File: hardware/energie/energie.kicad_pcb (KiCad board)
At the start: 2 copper layers, 102 x 87 mm, 86 parts, among them J1 transfos, J2 Conn_01x05_Pin, J3 linky, J4 Serial, J5 pilotes, J6 gpio, J7 I2C, J8 power, Q1 BSS123, Q2 BSS123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

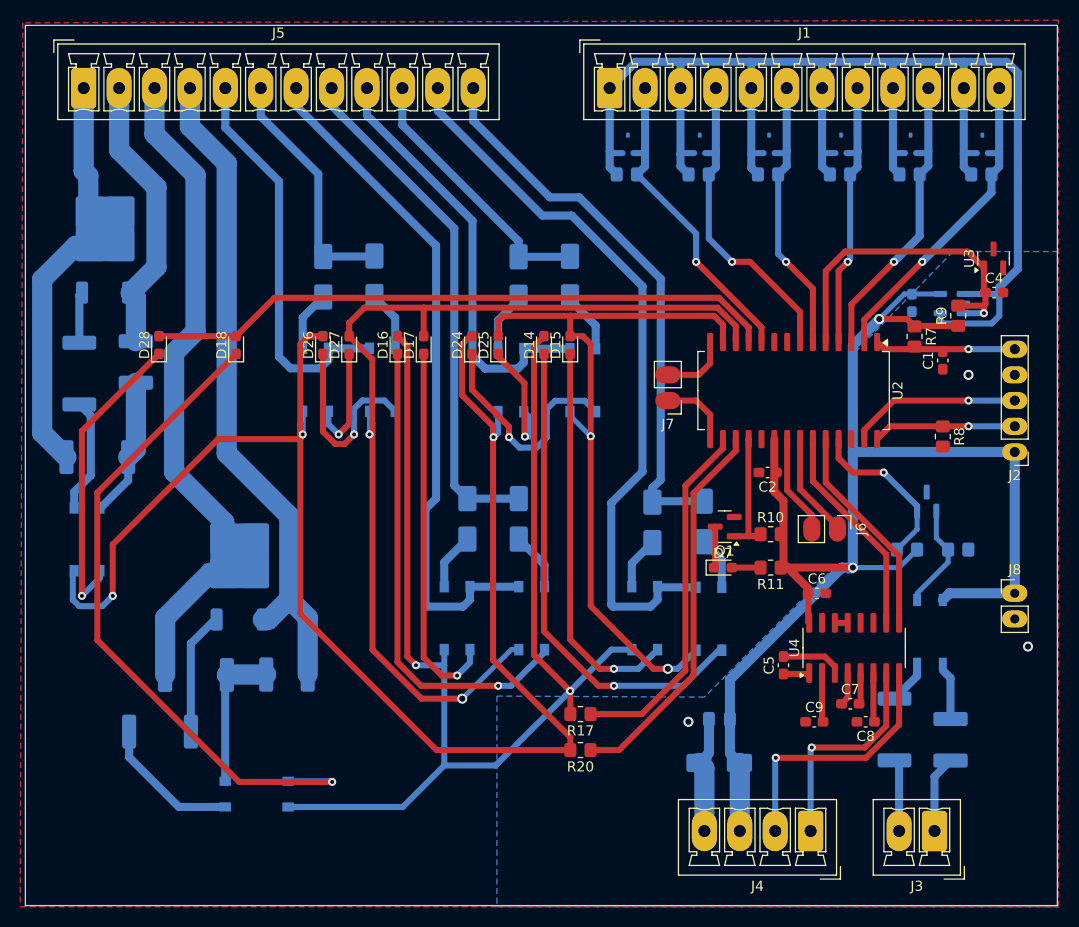
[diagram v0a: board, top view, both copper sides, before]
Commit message: energie: ajout d'une alimentation AC/DC pour que le module soit autonome (et que la connection à la centrale puisse être isolée)
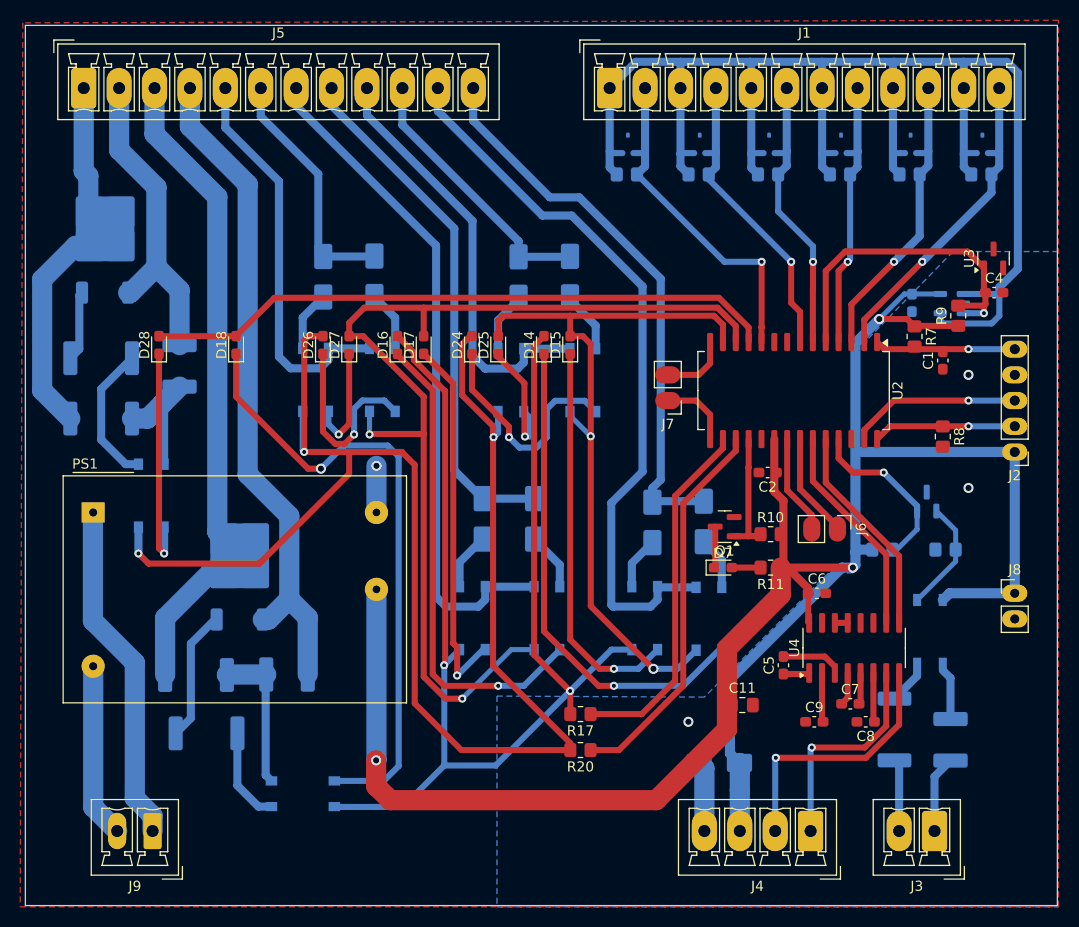
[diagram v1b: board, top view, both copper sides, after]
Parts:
- added J9: ACin, Connector_Phoenix_MC:PhoenixContact_MCV_1,5_2-G-3.5_1x02_P3.50mm_Vertical, F.Cu at (88.8, 130.4)
- added PS1: IRM-02-5, Converter_ACDC:Converter_ACDC_MeanWell_IRM-02-xx_THT, F.Cu at (82.9, 98.9)
- C11: moved to F.Cu
- moved U13 7.68 mm to (88.6, 97.3)
- moved R16 4.60 mm to (94.1, 120.8), turned to 0 degrees
- moved U8 4.57 mm to (103.6, 126.7)
- moved C13 4.33 mm to (91.4, 84.5)
- moved R18 3.83 mm to (83.7, 89.7)
- moved C11 2.66 mm to (147.1, 118.0), turned to 0 degrees
- moved R19 2.64 mm to (83.7, 83.7), turned to 0 degrees
- moved R12 2.43 mm to (160.9, 102.6), turned to 0 degrees
- moved U10 1.51 mm to (127.8, 109.4)
- moved U7 1.51 mm to (120.4, 109.4)
- moved D12 1.51 mm to (126.5, 99.6)
- moved D13 1.51 mm to (121.4, 99.6)
- moved R13 1.25 mm to (167.1, 102.6), turned to 180 degrees
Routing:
- net +5V: track 143.3 -> 213.3 mm, vias 2 -> 3
- net Net-(J9-Pin_1): track 0.00 -> 33.9 mm
- net Net-(J9-Pin_2): track 0.00 -> 17.3 mm
- net Net-(D28-K): track 30.3 -> 22.5 mm
- net /outputs/OB: track 98.0 -> 104.3 mm
- net Net-(D14-A): track 126.9 -> 121.4 mm
- net Net-(D18-K): track 67.4 -> 62.2 mm
- net Net-(R16-Pad2): track 14.1 -> 9.39 mm
- net Net-(D19-A1): track 27.8 -> 31.7 mm
- net Net-(D19-A2): track 36.9 -> 33.3 mm
- net Net-(R19-Pad2): track 11.4 -> 14.0 mm
- net Net-(J1-Pin_2): track 31.8 -> 33.9 mm
- net Net-(D19-G): track 5.06 -> 6.96 mm
- net Net-(C13-Pad2): track 13.9 -> 12.0 mm
- net Net-(D9-A2): track 62.5 -> 60.7 mm
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
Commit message: Utilise des emprumtes CMS pour deux connecteurs optionels.
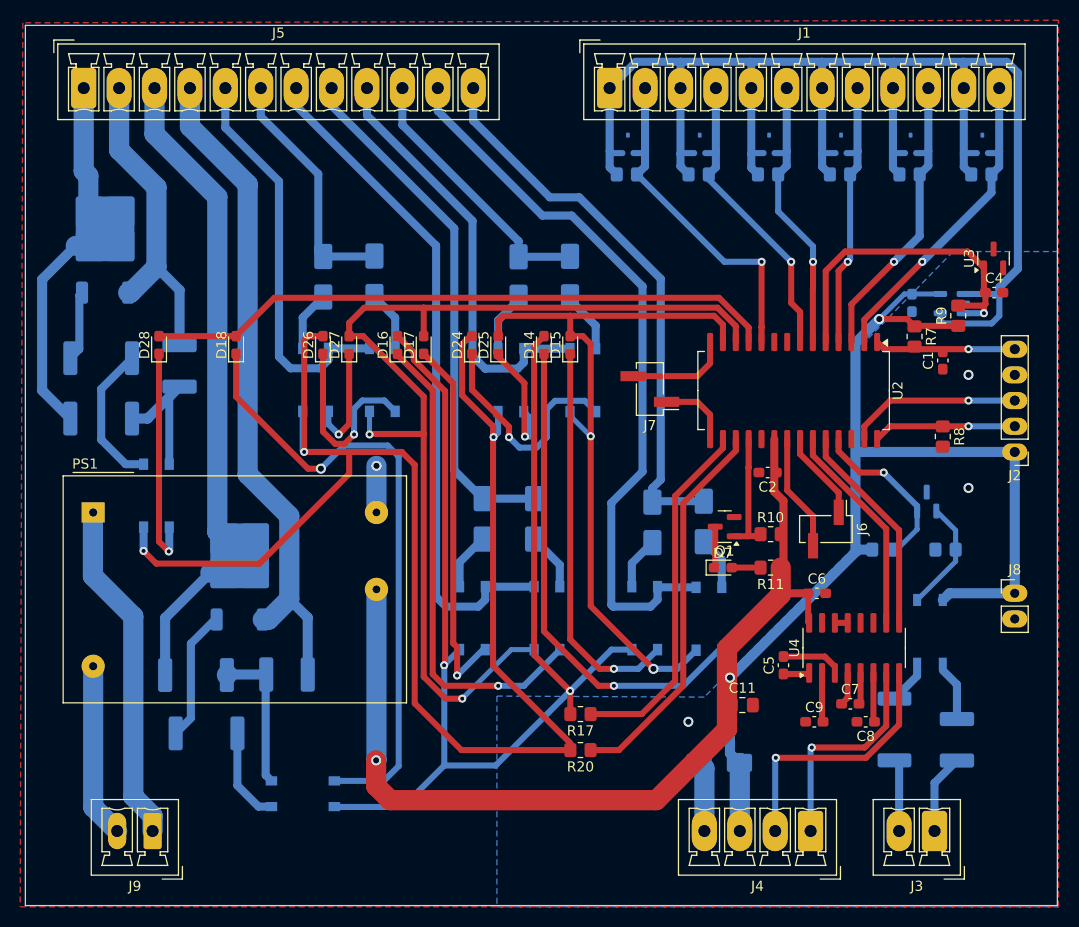
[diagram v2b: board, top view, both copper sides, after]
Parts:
- J6, J7: footprint Connector_PinHeader_2.54mm:PinHeader_1x02_P2.54mm_Vertical -> Connector_PinHeader_2.54mm:PinHeader_1x02_P2.54mm_Vertical_SMD_Pin1Left
- moved J7 2.11 mm to (137.9, 86.7)
- moved J6 1.14 mm to (155.3, 100.6)
- moved C10 0.64 mm to (168.3, 121.4)
- moved U13 0.51 mm to (89.2, 97.3)
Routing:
- net +5V: track 213.3 -> 208.3 mm
- net Net-(J7-Pin_2): track 6.77 -> 10.3 mm
- net Net-(C13-Pad2): track 12.0 -> 14.1 mm
- net Net-(J6-Pin_2): track 9.90 -> 11.6 mm
- net Net-(J6-Pin_1): track 10.2 -> 8.82 mm
- net Net-(D24-A): track 147.7 -> 147.1 mm
- net Net-(R19-Pad2): track 14.0 -> 14.5 mm

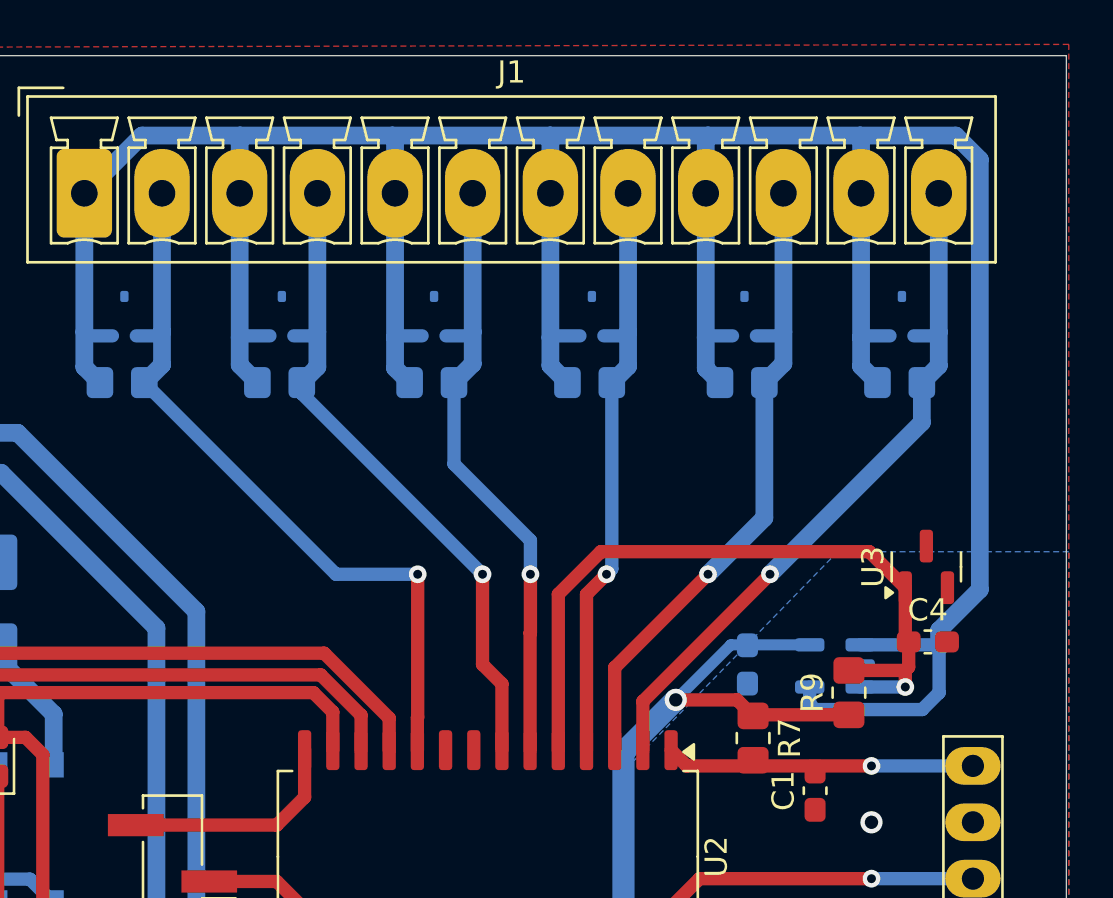
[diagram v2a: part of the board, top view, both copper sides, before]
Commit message: Remplace le MCP6006 par MCP6007 que l'on a en stock
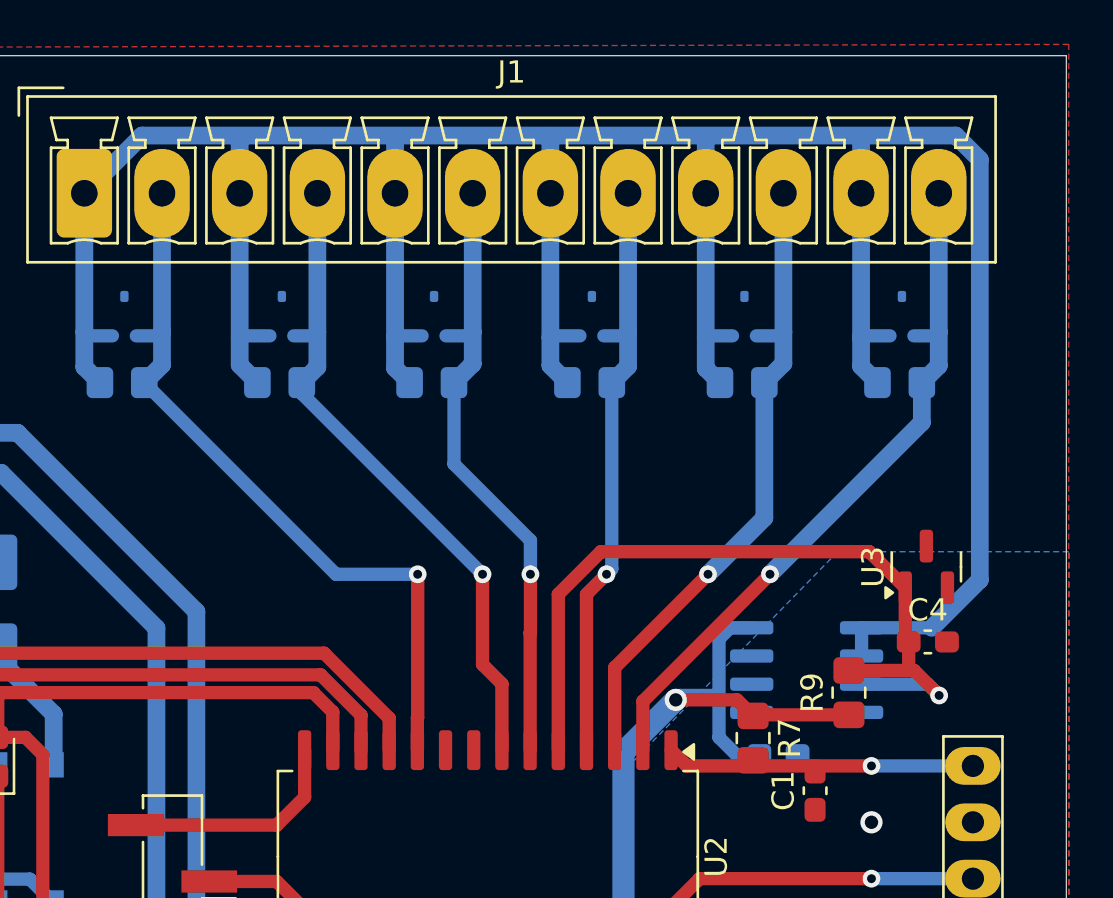
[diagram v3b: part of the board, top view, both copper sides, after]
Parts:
- U1: value MCP6006-OT -> MCP6007-xSN; footprint Package_TO_SOT_SMD:SOT-23-5 -> Package_SO:SOIC-8_3.9x4.9mm_P1.27mm
- moved C3 4.30 mm to (165.2, 82.3), turned to 180 degrees
- moved U1 1.29 mm to (166.5, 78.5)
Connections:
- C3 pad 1: +5V -> GND
- C3 pad 2: GND -> +5V
- U1 pad 2: GND -> Net-(J1-Pin_1)
- U1 pad 4: Net-(J1-Pin_1) -> GND
- U1 pad 5: +5V -> GND
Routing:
- net Net-(J1-Pin_1): track 151.1 -> 141.9 mm
- net +5V: track 208.3 -> 211.5 mm
- net Vref: track 33.1 -> 36.0 mm

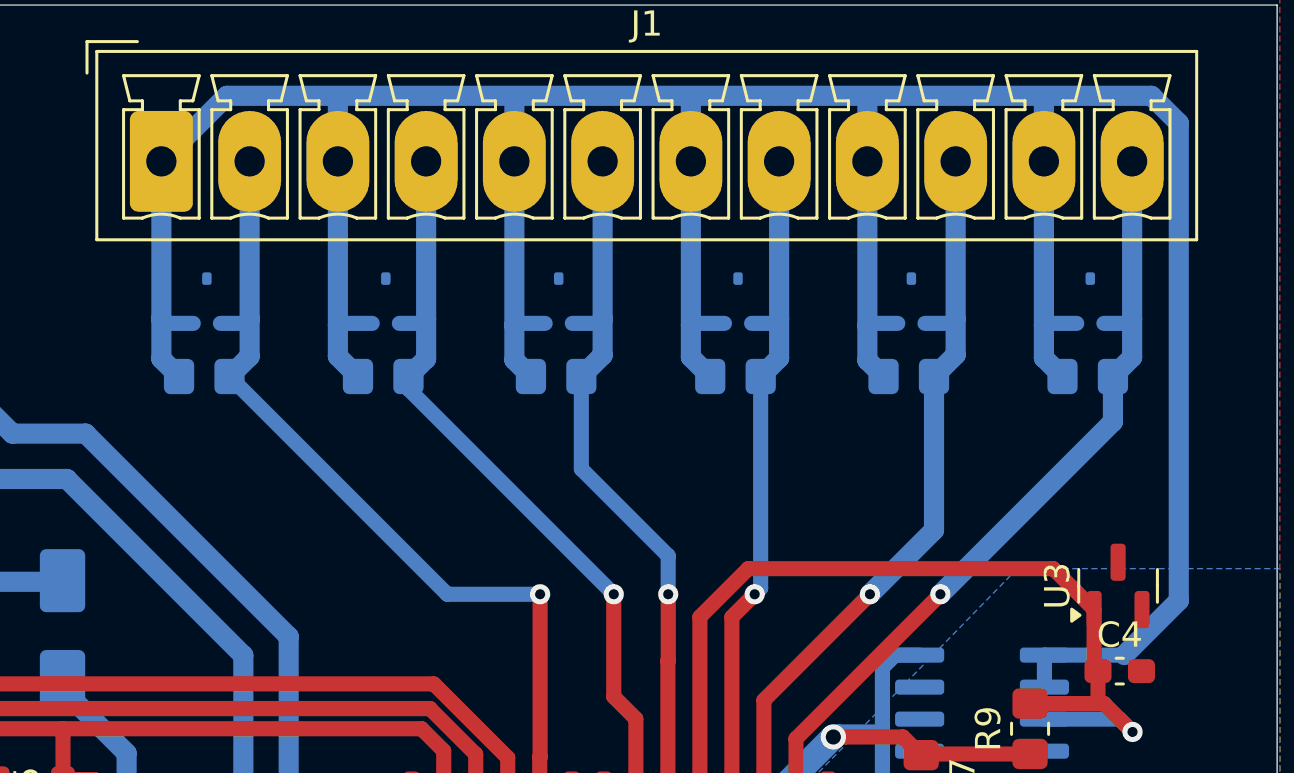
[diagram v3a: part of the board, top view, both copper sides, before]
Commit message: Remplace BZB984-C2V4 (non dispo) par BZB84-B2V7
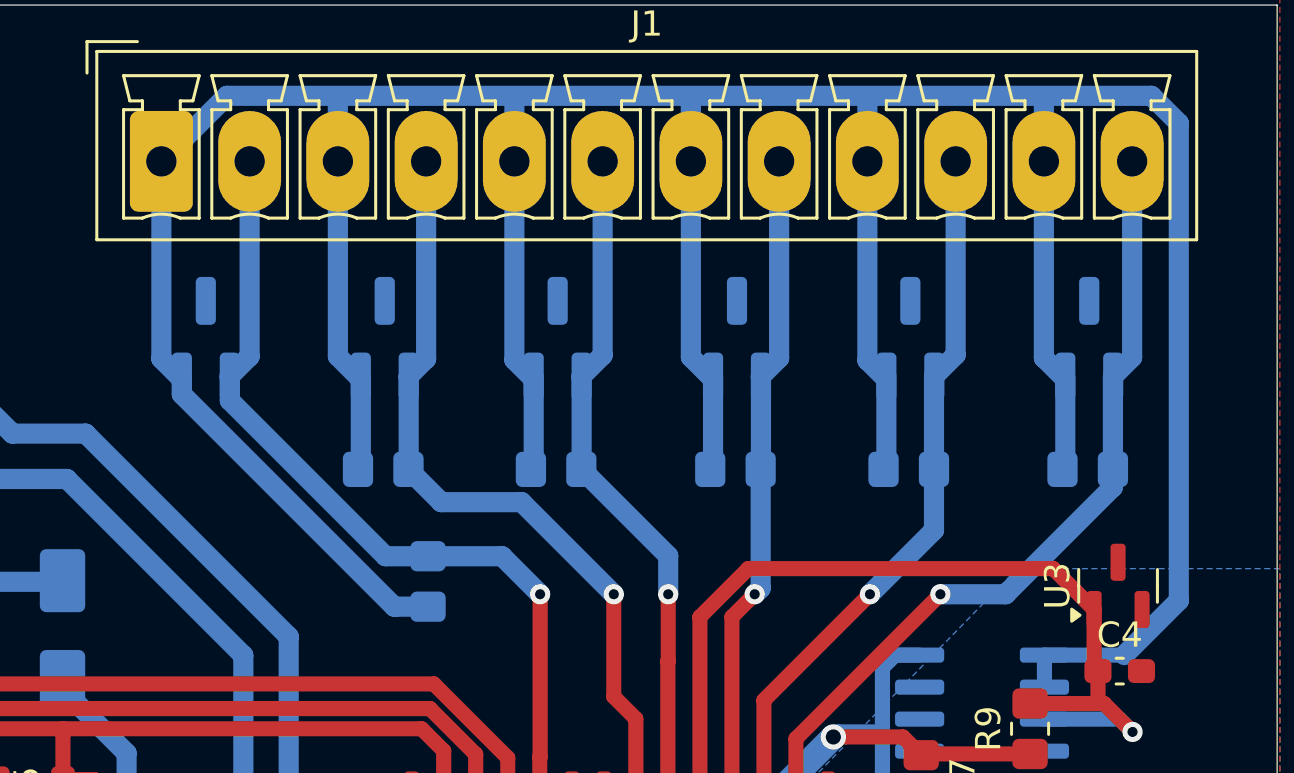
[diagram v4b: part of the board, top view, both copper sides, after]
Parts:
- D1, D2, D3, D4, D5, D6: value 2.4V -> 2.7V; footprint bouyer-smd.mod:SOT-663 -> Package_TO_SOT_SMD:SOT-23_Handsoldering
- moved R1 12.0 mm to (144.5, 73.7), turned to 90 degrees
- moved R2 3.68 mm to (142.7, 69.2)
- moved R3 3.68 mm to (149.6, 69.2)
- moved R4 3.68 mm to (156.7, 69.2)
- moved R5 3.68 mm to (163.6, 69.2)
- moved R6 3.68 mm to (170.7, 69.2)
- moved D1 1.46 mm to (135.7, 64.0)
- moved D2 1.46 mm to (142.8, 64.0)
- moved D4 1.46 mm to (156.8, 64.0)
- moved D5 1.46 mm to (163.7, 64.0)
- moved D6 1.46 mm to (170.7, 64.0)
- moved D3 1.46 mm to (149.7, 64.0)
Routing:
- net Net-(J1-Pin_1): track 141.9 -> 165.8 mm
- net Net-(J1-Pin_6): track 28.2 -> 26.9 mm
- net Net-(J1-Pin_10): track 29.5 -> 28.2 mm
- net Net-(J1-Pin_8): track 27.0 -> 25.9 mm
- net Net-(J1-Pin_4): track 30.3 -> 31.0 mm
- net Net-(J1-Pin_2): track 33.9 -> 33.2 mm
